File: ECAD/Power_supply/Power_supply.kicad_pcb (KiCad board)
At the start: 2 copper layers, 82.5 x 127 mm, 59 parts, among them J1 Barrel_Jack_Switch, J2 Conn_01x06, J3 Conn_01x02, Q1 DMP3037LSS-13, SW1 SW_Push_DPDT, U1 LM317_TO-220, U2 LM317_TO-220, U3 LM317_TO-220

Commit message: Minor change.
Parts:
- moved kibuzzard-67B50421 11.0 mm to (147.3, 150.4)
- moved D7 3.78 mm to (146.0, 155.6)
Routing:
- net Net-(D7-A): track 7.74 -> 5.41 mm

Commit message: Minor change.
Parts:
- moved kibuzzard-67B50421 2.57 mm to (144.8, 150.5)
- moved D7 2.54 mm to (143.5, 155.6)
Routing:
- net Net-(D7-A): track 5.41 -> 6.50 mm

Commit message: Fix alignment mistake.
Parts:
- moved kibuzzard-67B50421 1.30 mm to (146.1, 150.5)
- moved D7 1.27 mm to (144.8, 155.6)

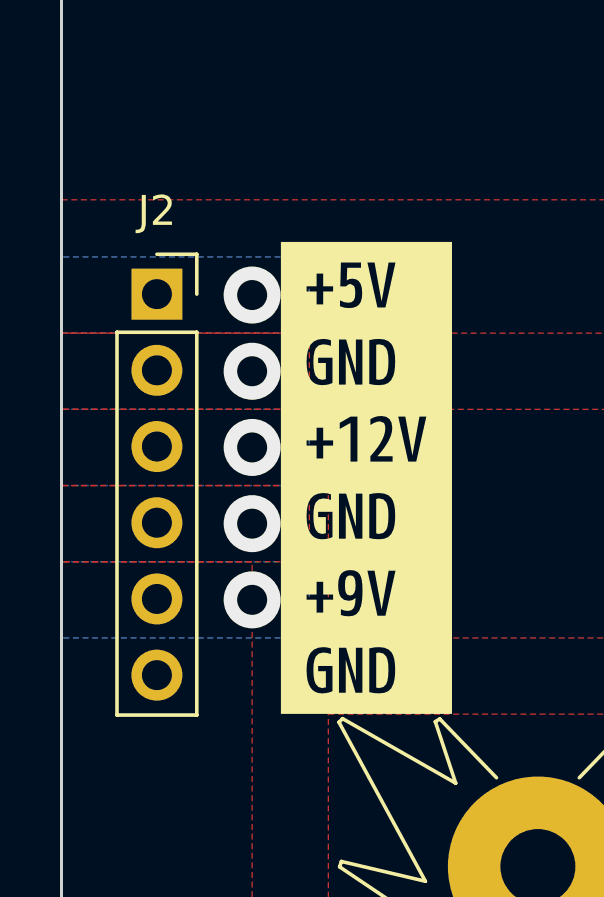
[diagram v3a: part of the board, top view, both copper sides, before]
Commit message: Minor alignment fix.
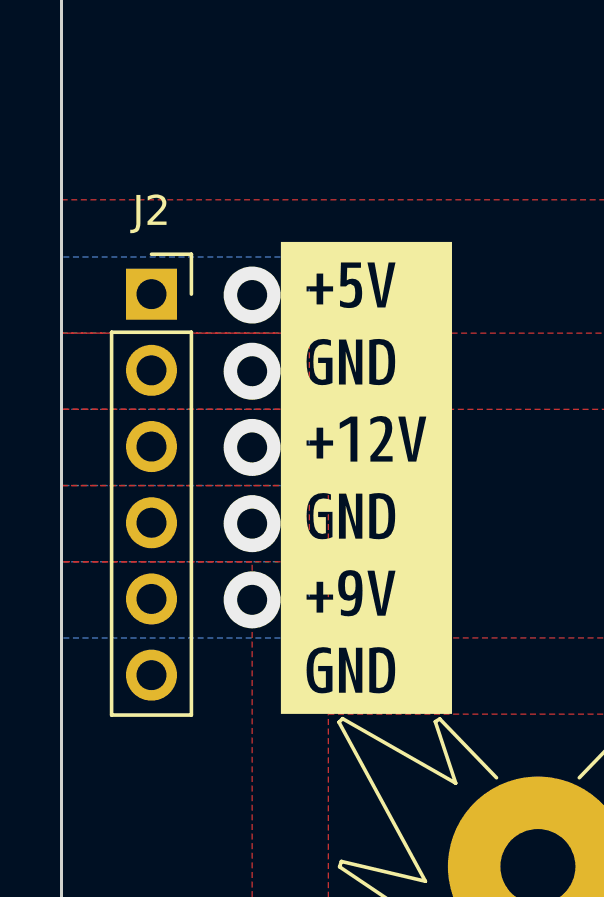
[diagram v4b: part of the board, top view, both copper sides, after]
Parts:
- moved J2 0.18 mm to (106.5, 105.4)
